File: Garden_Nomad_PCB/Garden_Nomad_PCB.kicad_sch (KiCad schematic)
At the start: 20 parts, among them J1 Battery In, PH In, Moisture I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, J4 OLED Sockets, J5 BME Sockets, J7 P2 Sockets Left, J8 P2 Sockets Right, SW1 Mode Button, SW2 Next Button, SW3 Sample Button, SW4 Water Alert Reset, SW5 Feed Alert Reset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

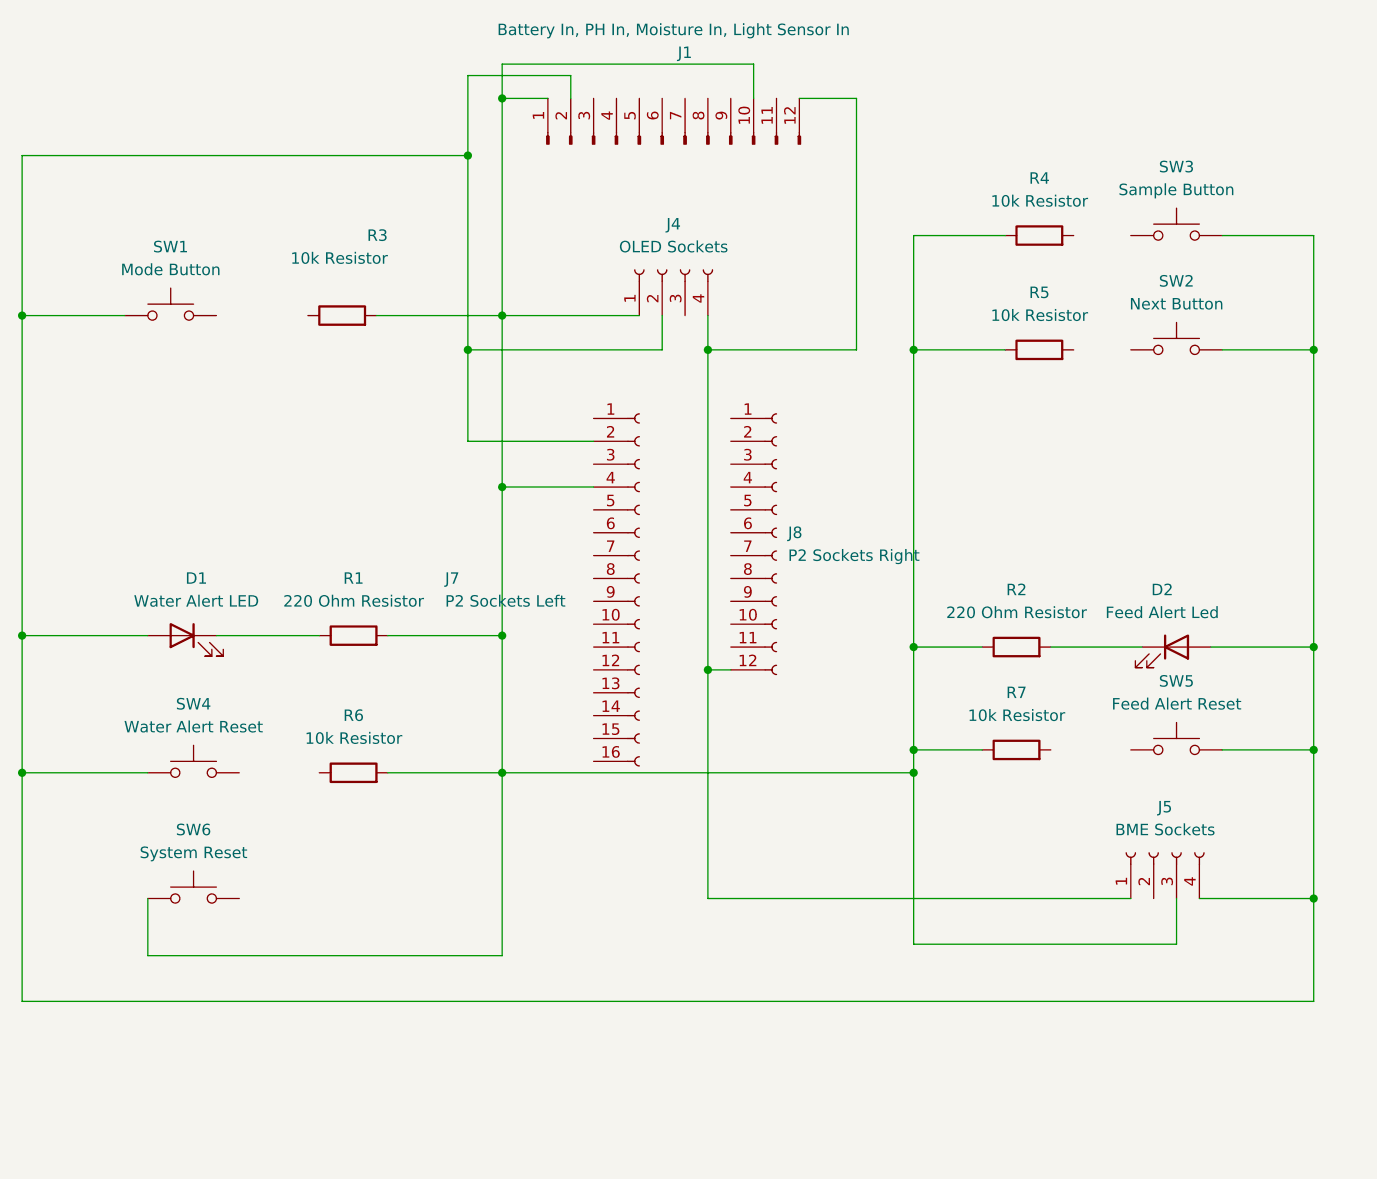
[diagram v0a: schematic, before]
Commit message: Commented code, lowered sleep duration (for now), added PDFs of all notes, finished PCB
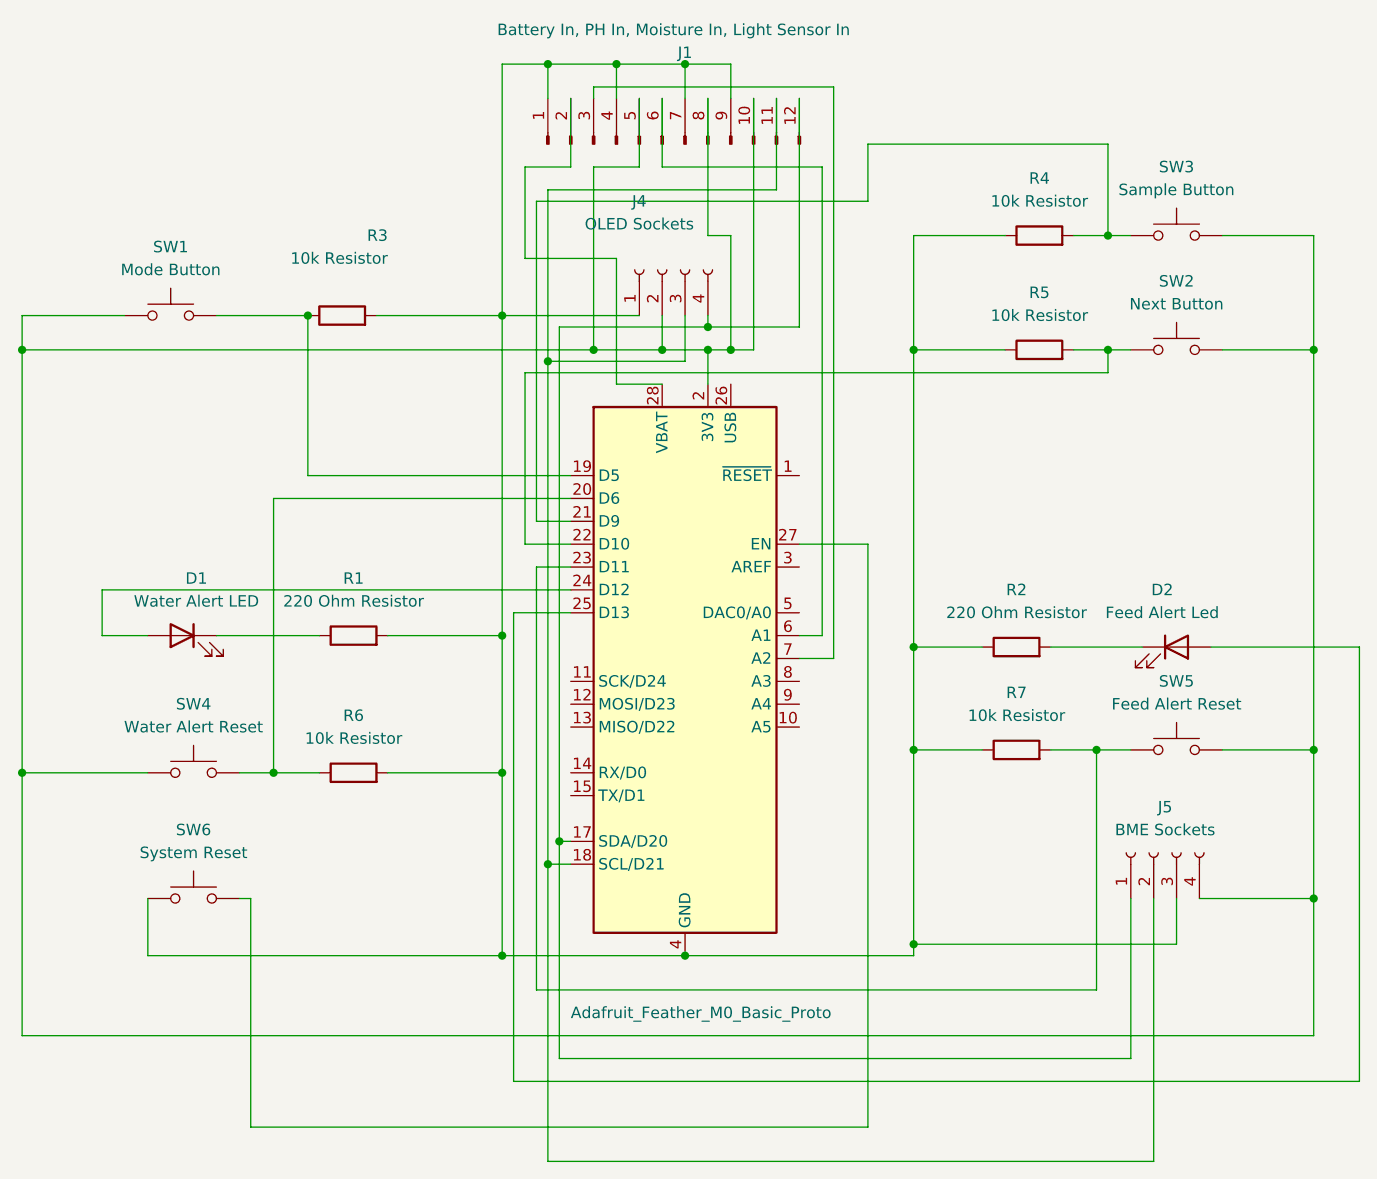
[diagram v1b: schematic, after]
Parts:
- removed J7: P2 Sockets Left, Connector_PinSocket_2.54mm:PinSocket_1x16_P2.54mm_Vertical, symbol Connector:Conn_01x16_Socket
- removed J8: P2 Sockets Right, Connector_PinSocket_2.54mm:PinSocket_1x12_P2.54mm_Vertical, symbol Connector:Conn_01x12_Socket
- added A1: Adafruit_Feather_M0_Basic_Proto, Module:Adafruit_Feather, symbol MCU_Module:Adafruit_Feather_M0_Basic_Proto
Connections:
- net at SW3.1: now also R4.2, A1.21 (D9)
- net at J4.2 (Pin_2), J5.4 (Pin_4), SW1.1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: now also J1.10 (Pin_10), J1.5 (Pin_5), J1.8 (Pin_8), A1.2 (3V3); no longer D1.2 (A), D2.2 (A), J1.2 (Pin_2)
- net at SW1.2: now also R3.1, A1.19 (D5)
- net at J1.12 (Pin_12), J4.4 (Pin_4), J5.1 (Pin_1): now also A1.17 (SDA/D20)
- net at R6.1: now also SW4.2, A1.20 (D6)
- net at J1.1 (Pin_1), J4.1 (Pin_1), J5.3 (Pin_3)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: now also J1.4 (Pin_4), J1.7 (Pin_7), J1.9 (Pin_9), A1.16 (GND), A1.4 (GND); no longer J1.10 (Pin_10)
- net at SW2.1: now also R5.2, A1.22 (D10)
- net at SW5.1: now also R7.2, A1.23 (D11)
- net at J1.11 (Pin_11): now also J4.3 (Pin_3), J5.2 (Pin_2), A1.18 (SCL/D21)
- net at J1.3 (Pin_3): now also A1.7 (A2)
- net at J1.6 (Pin_6): now also A1.6 (A1)
- net at SW6.2: now also A1.27 (EN)
- new net: A1.24 (D12), D1.2 (A)
- new net: A1.25 (D13), D2.2 (A)
- new net: A1.28 (VBAT), J1.2 (Pin_2)
